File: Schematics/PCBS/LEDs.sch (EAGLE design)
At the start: 20 parts, among them IC1 ATMEGA328P-AU, Q1 TRANSISTOR-FET_DMN2004K, Q2 TRANSISTOR-FET_DMN2004K, Q3 TRANSISTOR-FET_DMN2004K, Q4 TRANSISTOR-FET_DMN2004K, Q5 TRANSISTOR-FET_DMN2004K, Q6 TRANSISTOR-FET_DMN2004K, Q7 TRANSISTOR-FET_DMN2004K, Q8 TRANSISTOR-FET_DMN2004K, Q9 TRANSISTOR-FET_DMN2004K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

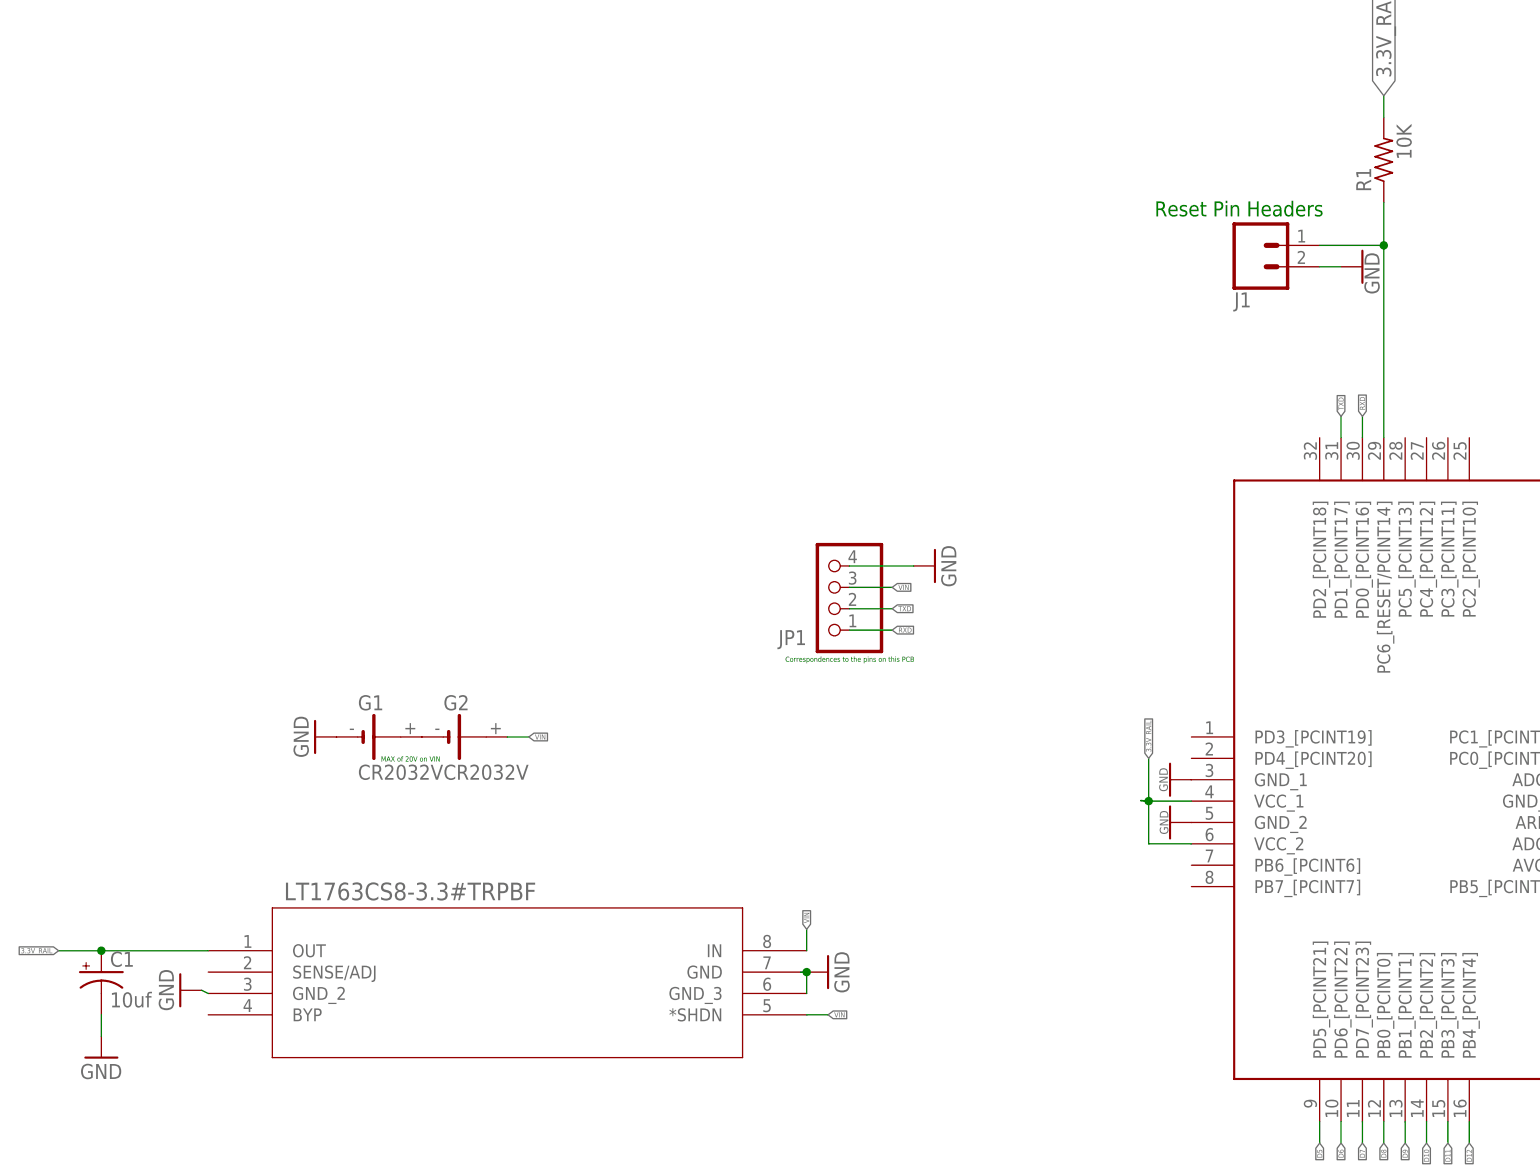
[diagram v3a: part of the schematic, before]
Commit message: started on Bidirectional Logic Level Converter
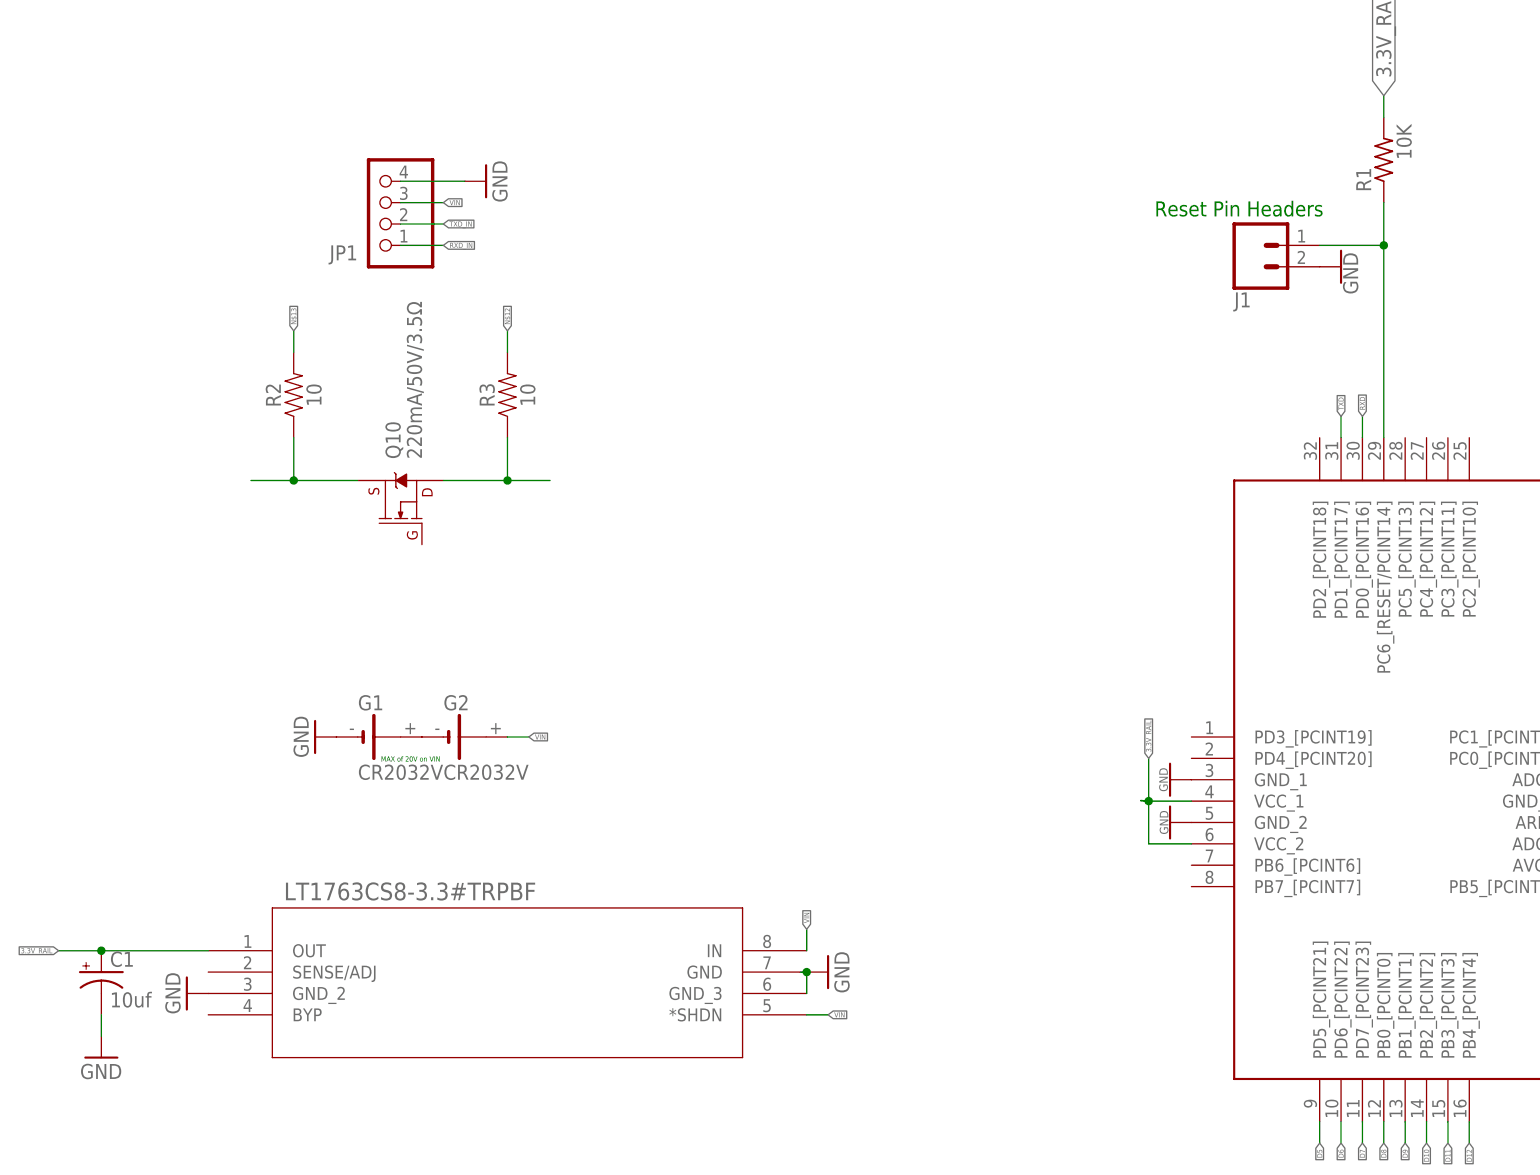
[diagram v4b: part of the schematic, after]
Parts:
- added Q10: 220mA/50V/3.5Ω, SparkFun-DiscreteSemi:MOSFET-NCH-BSS138
- added R2, R3: 10, SparkFun-Resistors:10OHM-HORIZ-1/4W-1%
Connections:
- new net N$10: Q10.D, R2.1
- new net N$11: Q10.S, R3.1
- new net N$12: R3.2
- new net N$13: R2.2
- new net RXD_IN: JP1.1
- new net TXD_IN: JP1.2
- net RXD: no longer JP1.1
- net TXD: no longer JP1.2
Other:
- note removed: "Correspondences to the pins on this PCB"
- moved on the sheet: JP1
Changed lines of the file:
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@@
 <part name="GND17" library="supply1" library_urn="urn:adsk.eagle:library:371" deviceset="GND" device=""/>
 <part name="GND18" library="supply1" library_urn="urn:adsk.eagle:library:371" deviceset="GND" device=""/>
+<part name="R2" library="SparkFun-Resistors" deviceset="10OHM" device="-HORIZ-1/4W-1%" value="10"/>
+<part name="R3" library="SparkFun-Resistors" deviceset="10OHM" device="-HORIZ-1/4W-1%" value="10"/>
+<part name="Q10" library="SparkFun-DiscreteSemi" deviceset="MOSFET-NCH" device="-BSS138" value="220mA/50V/3.5Ω"/>
 </parts>
 <sheets>
@@
 <text x="541.71" y="36.47" size="1.778" layer="91">Reset Pin Headers</text>
 <text x="449.78" y="-28.32" size="0.6096" layer="91">MAX of 20V on VIN</text>
-<text x="513.18" y="-15.86" size="0.6096" layer="91" rot="R180"> Correspondences to the pins on this PCB </text>
 </plain>
 <instances>
@@
 <attribute name="VALUE" x="414.02" y="-66.04" size="1.778" layer="96"/>
 </instance>
-<instance part="GND10" gate="1" x="425.94" y="-55.5" smashed="yes" rot="R270">
-<attribute name="VALUE" x="423.4" y="-52.96" size="1.778" layer="96" rot="R270"/>
+<instance part="GND10" gate="1" x="426.72" y="-55.88" smashed="yes" rot="R270">
+<attribute name="VALUE" x="424.18" y="-53.34" size="1.778" layer="96" rot="R270"/>
 </instance>
 <instance part="GND11" gate="1" x="543.56" y="-35.56" smashed="yes" rot="R270">
@@
 <attribute name="VALUE" x="542.28" y="-29.04" size="1.016" layer="96" rot="R270"/>
 </instance>
-<instance part="JP1" gate="A" x="502.92" y="-7.62" smashed="yes" rot="R180">
-<attribute name="NAME" x="500.38" y="-12.7" size="1.778" layer="95" rot="R180"/>
-<attribute name="VALUE" x="509.27" y="0" size="1.778" layer="96" rot="R180"/>
+<instance part="JP1" gate="A" x="449.58" y="38.1" smashed="yes" rot="R180">
+<attribute name="NAME" x="447.04" y="33.02" size="1.778" layer="95" rot="R180"/>
+<attribute name="VALUE" x="455.93" y="45.72" size="1.778" layer="96" rot="R180"/>
 </instance>
 <instance part="R1" gate="G$1" x="568.96" y="43.18" smashed="yes" rot="R90">
@@
 <attribute name="NAME" x="551.18" y="27.432" size="1.778" layer="95" font="vector" rot="MR180"/>
 </instance>
-<instance part="GND17" gate="1" x="566.42" y="30.48" smashed="yes" rot="R90">
-<attribute name="VALUE" x="568.452" y="27.178" size="1.778" layer="96" rot="R90"/>
-</instance>
-<instance part="GND18" gate="1" x="515.62" y="-5.08" smashed="yes" rot="R90">
-<attribute name="VALUE" x="518.16" y="-7.62" size="1.778" layer="96" rot="R90"/>
+<instance part="GND17" gate="1" x="563.88" y="30.48" smashed="yes" rot="R90">
+<attribute name="VALUE" x="565.912" y="27.178" size="1.778" layer="96" rot="R90"/>
+</instance>
+<instance part="GND18" gate="1" x="462.28" y="40.64" smashed="yes" rot="R90">
+<attribute name="VALUE" x="464.82" y="38.1" size="1.778" layer="96" rot="R90"/>
+</instance>
+<instance part="R2" gate="G$1" x="439.42" y="15.24" smashed="yes" rot="R90">
+<attribute name="NAME" x="437.896" y="15.24" size="1.778" layer="95" font="vector" rot="R90" align="bottom-center"/>
+<attribute name="VALUE" x="440.944" y="15.24" size="1.778" layer="96" font="vector" rot="R90" align="top-center"/>
+</instance>
+<instance part="R3" gate="G$1" x="464.82" y="15.24" smashed="yes" rot="R90">
+<attribute name="NAME" x="463.296" y="15.24" size="1.778" layer="95" font="vector" rot="R90" align="bottom-center"/>
+<attribute name="VALUE" x="466.344" y="15.24" size="1.778" layer="96" font="vector" rot="R90" align="top-center"/>
+</instance>
+<instance part="Q10" gate="NMOS" x="452.12" y="2.54" smashed="yes" rot="R90">
+<attribute name="NAME" x="452.12" y="7.62" size="1.778" layer="95" font="vector" rot="R90"/>
+<attribute name="VALUE" x="454.66" y="7.62" size="1.778" layer="96" font="vector" rot="R90"/>
 </instance>
 </instances>
@@
 <segment>
 <pinref part="GND10" gate="1" pin="GND"/>
-<wire x1="428.48" y1="-55.5" x2="429.26" y2="-55.88" width="0.1524" layer="91"/>
 <pinref part="U1" gate="A" pin="GND_2"/>
 </segment>
@@
 <pinref part="J1" gate="G$1" pin="2"/>
 <pinref part="GND17" gate="1" pin="GND"/>
-<wire x1="561.34" y1="30.48" x2="563.88" y2="30.48" width="0.1524" layer="91"/>
 </segment>
 <segment>
@@
 <pinref part="JP1" gate="A" pin="4"/>
 <pinref part="GND18" gate="1" pin="GND"/>
-<wire x1="505.46" y1="-5.08" x2="513.08" y2="-5.08" width="0.1524" layer="91"/>
+<wire x1="452.12" y1="40.64" x2="459.74" y2="40.64" width="0.1524" layer="91"/>
 </segment>
 </net>
@@
 </segment>
 <segment>
+<pinref part="JP1" gate="A" pin="3"/>
+<wire x1="452.12" y1="38.1" x2="457.2" y2="38.1" width="0.1524" layer="91"/>
+<label x="457.2" y="38.1" size="0.6096" layer="95" xref="yes"/>
+</segment>
+<segment>
 <pinref part="U1" gate="A" pin="IN"/>
 <wire x1="500.38" y1="-50.8" x2="500.38" y2="-48.26" width="0.1524" layer="91"/>
@@
 <label x="502.92" y="-58.42" size="0.6096" layer="95" xref="yes"/>
 </segment>
-<segment>
-<pinref part="JP1" gate="A" pin="3"/>
-<wire x1="505.46" y1="-7.62" x2="510.54" y2="-7.62" width="0.1524" layer="91"/>
-<label x="510.54" y="-7.62" size="0.6096" layer="95" xref="yes"/>
-</segment>
 </net>
 <net name="N$19" class="0">
@@
 <label x="563.88" y="12.7" size="0.6096" layer="95" rot="R90" xref="yes"/>
 </segment>
-<segment>
-<pinref part="JP1" gate="A" pin="2"/>
-<wire x1="505.46" y1="-10.16" x2="510.54" y2="-10.16" width="0.1524" layer="91"/>
-<label x="510.54" y="-10.16" size="0.6096" layer="95" xref="yes"/>
-</segment>
 </net>
 <net name="RXD" class="0">
@@
 <wire x1="566.42" y1="10.16" x2="566.42" y2="12.7" width="0.1524" layer="91"/>
 <label x="566.42" y="12.7" size="0.6096" layer="95" rot="R90" xref="yes"/>
-</segment>
-<segment>
-<pinref part="JP1" gate="A" pin="1"/>
-<wire x1="505.46" y1="-12.7" x2="510.54" y2="-12.7" width="0.1524" layer="91"/>
-<label x="510.54" y="-12.7" size="0.6096" layer="95" xref="yes"/>
 </segment>
 </net>
@@
 </segment>
 </net>
+<net name="TXD_IN" class="0">
+<segment>
+<pinref part="JP1" gate="A" pin="2"/>
+<wire x1="452.12" y1="35.56" x2="457.2" y2="35.56" width="0.1524" layer="91"/>
+<label x="457.2" y="35.56" size="0.6096" layer="95" xref="yes"/>
+</segment>
+</net>
+<net name="RXD_IN" class="0">
+<segment>
+<pinref part="JP1" gate="A" pin="1"/>
+<wire x1="452.12" y1="33.02" x2="457.2" y2="33.02" width="0.1524" layer="91"/>
+<label x="457.2" y="33.02" size="0.6096" layer="95" xref="yes"/>
+</segment>
+</net>
+<net name="N$10" class="0">
+<segment>
+<pinref part="R2" gate="G$1" pin="1"/>
+<wire x1="447.04" y1="5.08" x2="439.42" y2="5.08" width="0.1524" layer="91"/>
+<wire x1="439.42" y1="5.08" x2="439.42" y2="10.16" width="0.1524" layer="91"/>
+<wire x1="439.42" y1="5.08" x2="434.34" y2="5.08" width="0.1524" layer="91"/>
+<junction x="439.42" y="5.08"/>
+<pinref part="Q10" gate="NMOS" pin="D"/>
+</segment>
+</net>
+<net name="N$11" class="0">
+<segment>
+<pinref part="R3" gate="G$1" pin="1"/>
+<wire x1="457.2" y1="5.08" x2="464.82" y2="5.08" width="0.1524" layer="91"/>
+<wire x1="464.82" y1="5.08" x2="464.82" y2="10.16" width="0.1524" layer="91"/>
+<wire x1="464.82" y1="5.08" x2="469.9" y2="5.08" width="0.1524" layer="91"/>
+<junction x="464.82" y="5.08"/>
+<pinref part="Q10" gate="NMOS" pin="S"/>
+</segment>
+</net>
+<net name="N$12" class="0">
+<segment>
+<pinref part="R3" gate="G$1" pin="2"/>
+<label x="464.82" y="22.86" size="0.6096" layer="95" rot="R90" xref="yes"/>
+<wire x1="464.82" y1="20.32" x2="464.82" y2="22.86" width="0.1524" layer="91"/>
+</segment>
+</net>
+<net name="N$13" class="0">
+<segment>
+<pinref part="R2" gate="G$1" pin="2"/>
+<wire x1="439.42" y1="20.32" x2="439.42" y2="22.86" width="0.1524" layer="91"/>
+<label x="439.42" y="22.86" size="0.6096" layer="95" rot="R90" xref="yes"/>
+</segment>
+</net>
 </nets>
 </sheet>
 </sheets>
+<errors>
+</errors>
 </schematic>
 </drawing>

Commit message: Added RXD Logic level converter && IO update
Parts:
- removed G1, G2: CR2032V, battery:CR2032V
- removed J1: (no value), SparkFun-Connectors:CONN_02
- added E1, E2: DPADS_PAD-0400-S, 52101-101-REV-A:DPADS_PAD-0400-S
- JP1: device pinhead:PINHD-1X4 -> adafruit:PINHD-1X8CLEANBIG
- R2, R3: value 10 -> 10K
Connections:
- removed net N$10: Q10.D, R2.1
- removed net N$11: Q10.S, R3.1
- removed net N$12: R3.2
- removed net N$13: R2.2
- removed net N$19: G1.+, G2.-
- removed net TXD_IN: JP1.2
- new net 2BD: JP1.1, JP1.2
- new net 3.3_RAIL: JP1.5
- new net 5V_RAIL: JP1.6, R2.2
- net 3.3V_RAIL: now also Q10.G, R3.2
- net GND: now also E2.P, JP1.8; no longer G1.-, J1.2, JP1.4
- net N$15: now also E1.P; no longer J1.1
- net RXD: now also Q10.S, R3.1
- net RXD_IN: now also JP1.3, Q10.D, R2.1; no longer JP1.1
- net TXD: now also JP1.4
- net VIN: now also JP1.7; no longer G2.+, JP1.3
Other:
- note added: "max 20V"
- note removed: "MAX of 20V on VIN"
- moved on the sheet: R2, R3

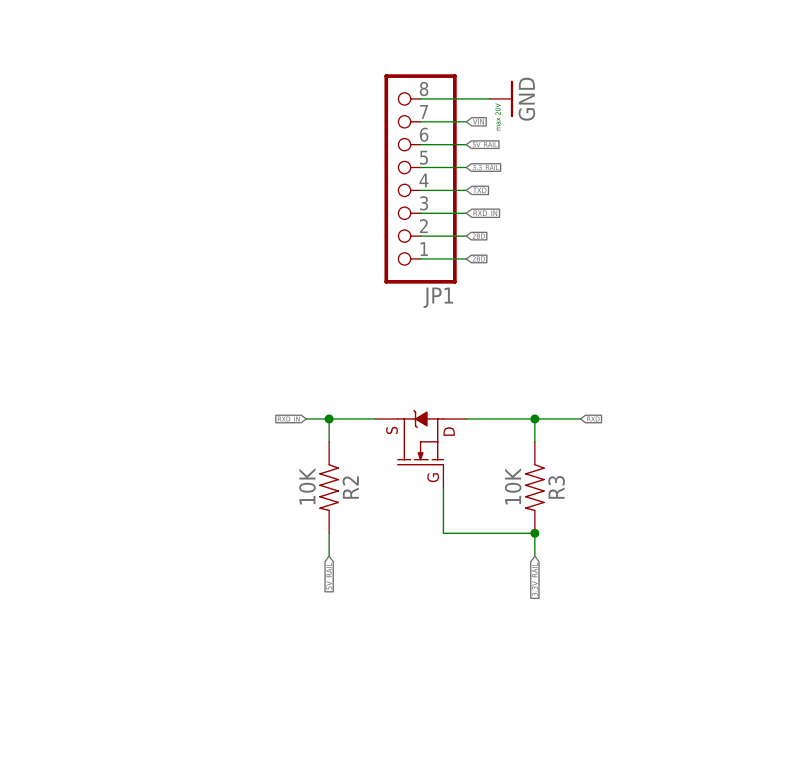
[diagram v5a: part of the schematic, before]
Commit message: updated RXD_IN 5v to 3.3v
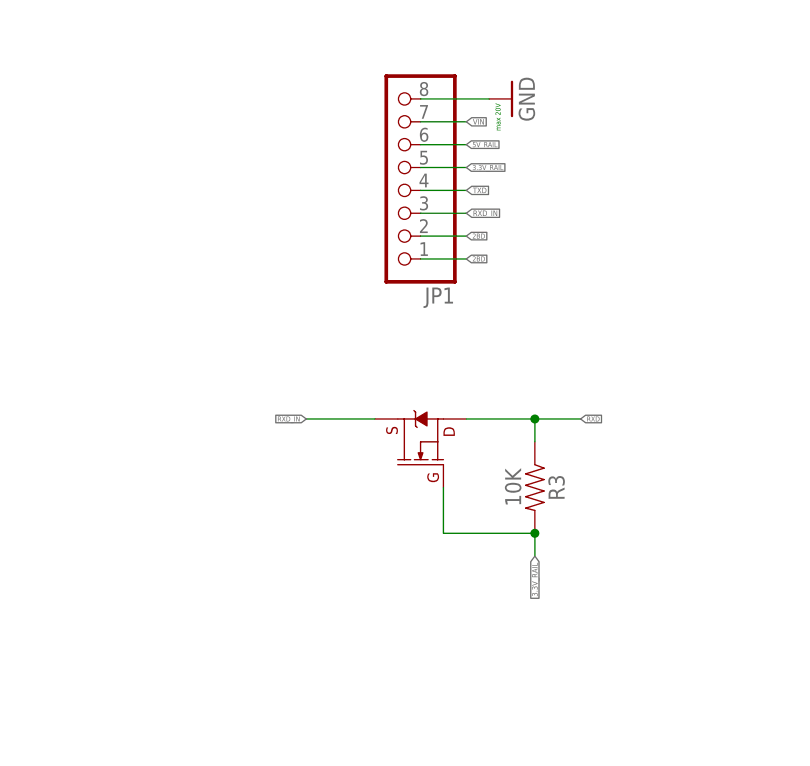
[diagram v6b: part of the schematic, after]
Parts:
- removed R2: 10K, SparkFun-Resistors:10OHM-HORIZ-1/4W-1%
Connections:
- removed net 3.3_RAIL: JP1.5
- net 3.3V_RAIL: now also JP1.5
- net 5V_RAIL: no longer R2.2
- net RXD_IN: no longer R2.1
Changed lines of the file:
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@@
 <part name="GND17" library="supply1" library_urn="urn:adsk.eagle:library:371" deviceset="GND" device=""/>
 <part name="GND18" library="supply1" library_urn="urn:adsk.eagle:library:371" deviceset="GND" device=""/>
-<part name="R2" library="SparkFun-Resistors" deviceset="10OHM" device="-HORIZ-1/4W-1%" value="10K"/>
 <part name="R3" library="SparkFun-Resistors" deviceset="10OHM" device="-HORIZ-1/4W-1%" value="10K"/>
 <part name="Q10" library="SparkFun-DiscreteSemi" deviceset="MOSFET-NCH" device="-BSS138" value="220mA/50V/3.5Ω"/>
@@
 <attribute name="VALUE" x="464.82" y="38.1" size="1.778" layer="96" rot="R90"/>
 </instance>
-<instance part="R2" gate="G$1" x="441.96" y="-2.54" smashed="yes" rot="R270">
-<attribute name="NAME" x="443.484" y="-2.54" size="1.778" layer="95" font="vector" rot="R270" align="bottom-center"/>
-<attribute name="VALUE" x="440.436" y="-2.54" size="1.778" layer="96" font="vector" rot="R270" align="top-center"/>
-</instance>
 <instance part="R3" gate="G$1" x="464.82" y="-2.54" smashed="yes" rot="R270">
 <attribute name="NAME" x="466.344" y="-2.54" size="1.778" layer="95" font="vector" rot="R270" align="bottom-center"/>
@@
 <junction x="464.82" y="-7.62"/>
 </segment>
+<segment>
+<wire x1="452.12" y1="33.02" x2="457.2" y2="33.02" width="0.1524" layer="91"/>
+<label x="457.2" y="33.02" size="0.5588" layer="95" xref="yes"/>
+<pinref part="JP1" gate="G$1" pin="5"/>
+</segment>
 </net>
 <net name="GND" class="0">
@@
 </segment>
 <segment>
-<pinref part="R2" gate="G$1" pin="1"/>
-<wire x1="447.04" y1="5.08" x2="441.96" y2="5.08" width="0.1524" layer="91"/>
-<wire x1="441.96" y1="5.08" x2="441.96" y2="2.54" width="0.1524" layer="91"/>
-<wire x1="441.96" y1="5.08" x2="439.42" y2="5.08" width="0.1524" layer="91"/>
-<junction x="441.96" y="5.08"/>
+<wire x1="447.04" y1="5.08" x2="439.42" y2="5.08" width="0.1524" layer="91"/>
 <pinref part="Q10" gate="NMOS" pin="D"/>
 <label x="439.42" y="5.08" size="0.5588" layer="95" rot="R180" xref="yes"/>
@@
 </net>
 <net name="5V_RAIL" class="0">
-<segment>
-<pinref part="R2" gate="G$1" pin="2"/>
-<wire x1="441.96" y1="-7.62" x2="441.96" y2="-10.16" width="0.1524" layer="91"/>
-<label x="441.96" y="-10.16" size="0.6096" layer="95" rot="R270" xref="yes"/>
-</segment>
 <segment>
 <wire x1="452.12" y1="35.56" x2="457.2" y2="35.56" width="0.1524" layer="91"/>
@@
 </segment>
 </net>
-<net name="3.3_RAIL" class="0">
-<segment>
-<wire x1="452.12" y1="33.02" x2="457.2" y2="33.02" width="0.1524" layer="91"/>
-<label x="457.2" y="33.02" size="0.5588" layer="95" xref="yes"/>
-<pinref part="JP1" gate="G$1" pin="5"/>
-</segment>
-</net>
